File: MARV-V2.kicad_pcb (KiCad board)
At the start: 4 copper layers, 50.7 x 45.5 mm, 107 parts, among them J10 DBG pads (SWCLK SWDIO GND), J11 microSD, Molex 47219-2001 loc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, J3 ESC pads (CURR TX M4 M3 M2 M1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, J4 USB_C_PROGRAM_POWER, J6 IO array signal column (inner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, J7 IO array power column (5V / 3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, J8 IO array GND column (board ed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, Q1 AO3401A, SW1 RESET (RUN to GND), SW2 BOOTSEL (via R24), U12 TPS7A2033PDBVR, U20 RP2354B, U21 ICM-45686 6-axis IMU, U22 BMP581 barometer, U23 ADXL375 high-g accelerometer, U24 DNP: W25Q32JVSNIQ, 32 Mbit QS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, U7 AP63203WU-7, Y1 12 MHz TAXM12M4RFBCCT2T, CL 1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

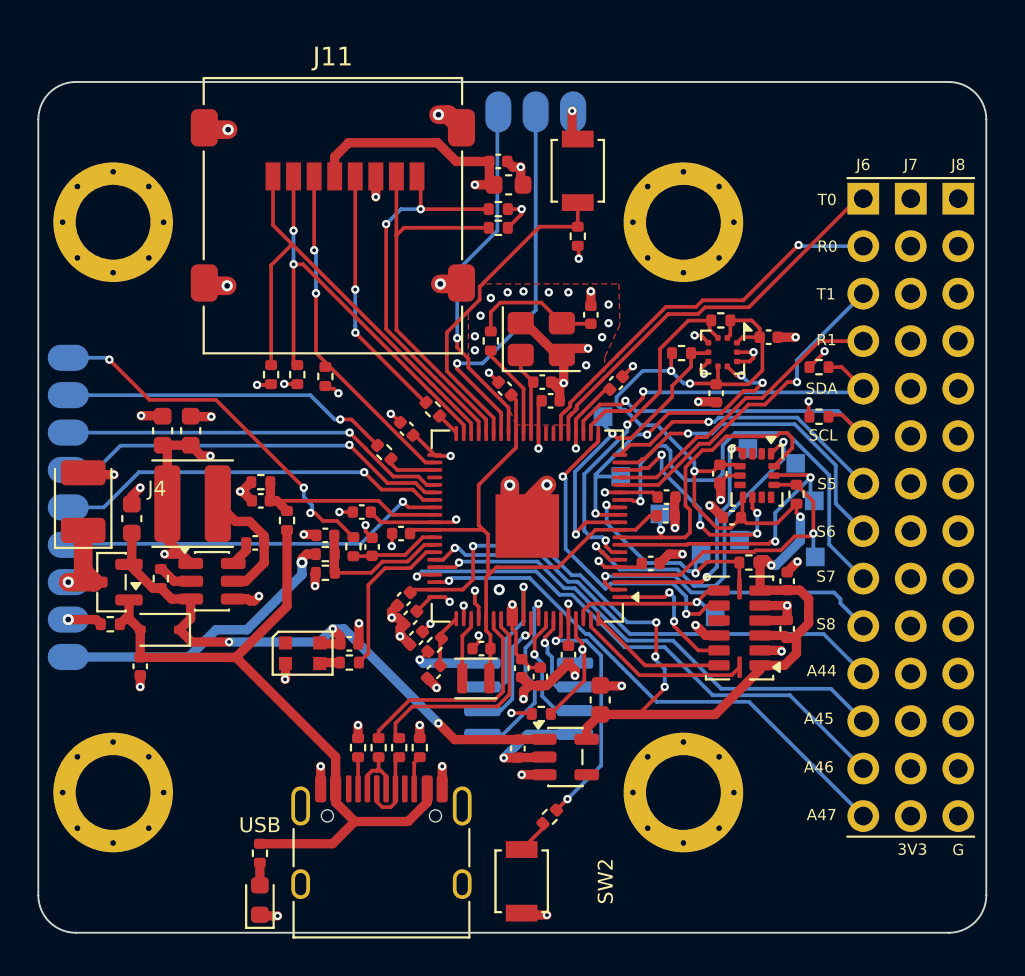
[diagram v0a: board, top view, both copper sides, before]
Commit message: Normalise silkscreen for JLC, reorder MCU GPIOs, relax DFM guards
- Silk strokes 0.15 mm, silk text 1.0/0.15 mm, no outlines on 0402 R/C and L2,
  compact no-silk test-point footprint (MARV_Packages), edge-connector silk
  trimmed inside the outline, one dangling GND via removed;
  lib_footprint_mismatch set to ignore in the DFM profile and documented.
- MCU pin order: SD bus on GPIO28-33 (top-left corner), ESC row in J3 pad order
  (TELEM GPIO34, PWM4-1 GPIO36-39, CURR ADC1, VBAT ADC2), LED_DATA GPIO43;
  GPIO26/27/35 no-connect. PINOUT.md, DESIGN_SPEC.md and the netlist checker
  follow.
- IO block J7 rows 7-10 moved from 5V_IN to V3V3_SYS (no servo power from FC).
- DFM: courtyard rules relaxed to JLC body-to-body equivalents, no-surcharge via
  presets 0.45/0.20, 0.50/0.25, 0.60/0.30, via-in-pad rule exempts the back-side
  hand-solder rows J3/J10.

Co-Authored-By: Claude Fable 5.1 <noreply@anthropic.com>
Claude-Session: https://claude.ai/code/session_01VST8gLViyNpcDEYyh3itUW
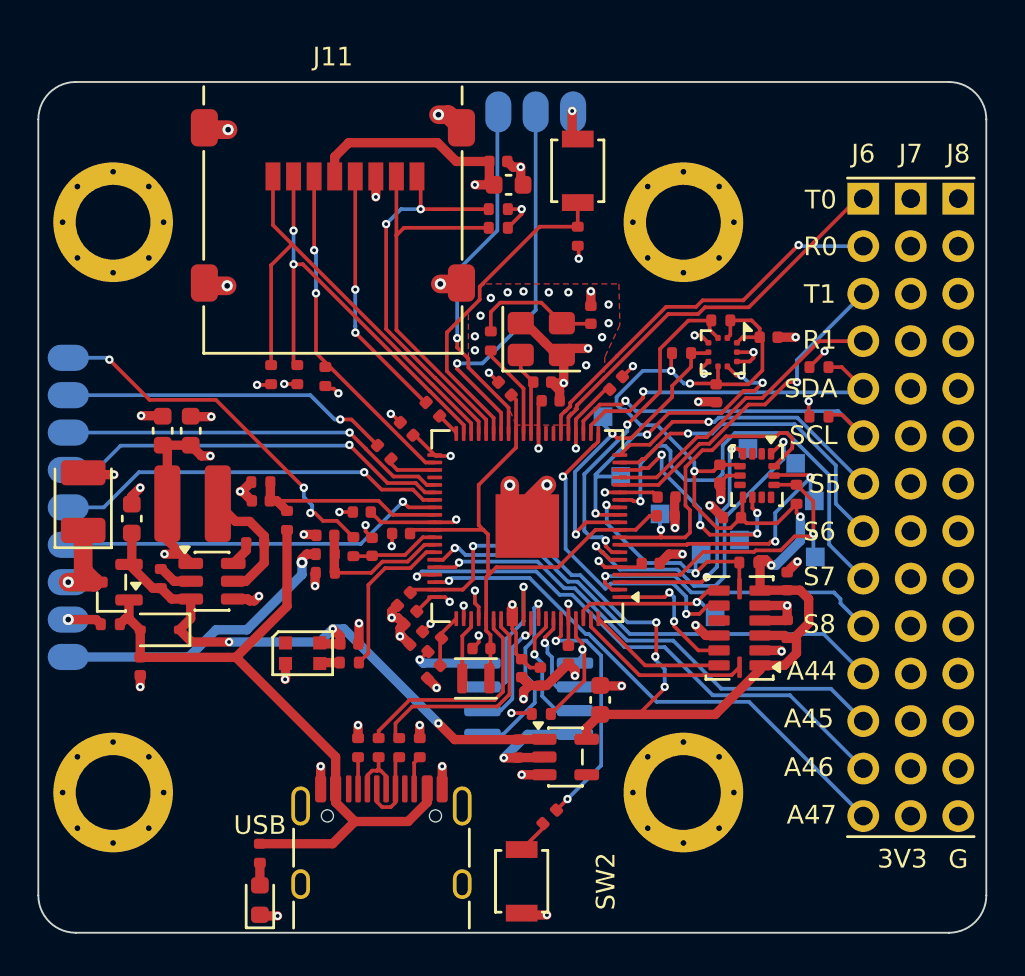
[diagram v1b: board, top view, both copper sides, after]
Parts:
- TP1, TP10, TP2, TP3, TP4, TP5, TP6, TP7, TP8, TP9: footprint TestPoint:TestPoint_Pad_1.0x1.0mm -> MARV_Packages:TestPoint_Pad_1.0x1.0mm_Compact
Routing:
- net GND: vias 71 -> 70

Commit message: Order-ready: U24 via cleared, R58 sourced (C25092), fab and assembly exports
- Owner moved the GND via out of U24's pad column: DRC now has no electrical
  errors, 0 unconnected, 0 schematic-parity issues (78 cosmetic courtyard
  gaps and 80 RP2350 pad-size review warnings remain).
- R58 22 ohm 0402 gets LCSC C25092 in the schematic, the footprint field and
  tools/jlc/lcsc_map.csv.
- build/ (ignored) holds Gerbers+drill (build/MARV-V2-gerbers.zip) and the
  JLC BOM/CPL (build/assembly/) generated from this commit.

Co-Authored-By: Claude Fable 5.1 <noreply@anthropic.com>
Claude-Session: https://claude.ai/code/session_01VST8gLViyNpcDEYyh3itUW
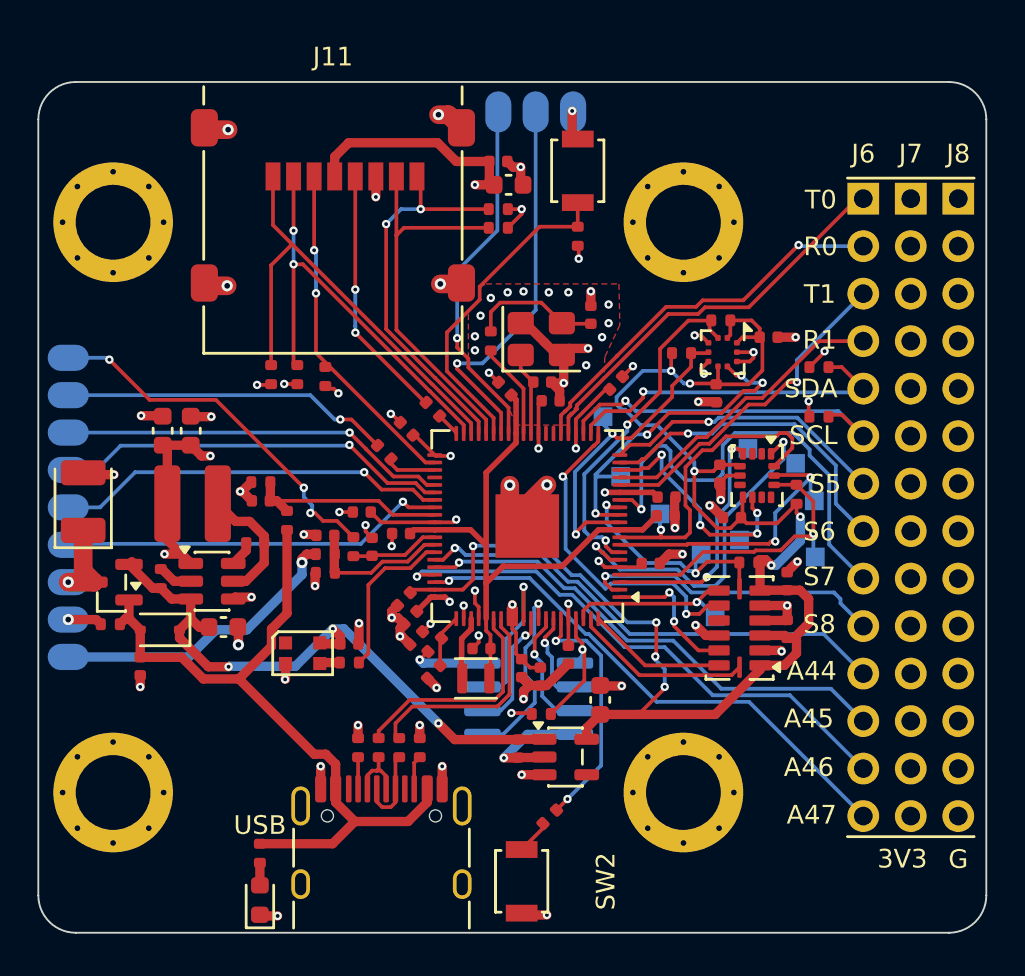
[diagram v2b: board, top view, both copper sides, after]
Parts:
- moved C8 7.59 mm to (84.5, 106.4), turned to 0 degrees
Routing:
- net GND: track 85.9 -> 84.5 mm, vias 70 -> 69
- net V5_SYS: track 32.3 -> 33.3 mm
- net USB_VBUS: track 39.0 -> 39.9 mm
- net PWM7: track 24.0 -> 24.8 mm
